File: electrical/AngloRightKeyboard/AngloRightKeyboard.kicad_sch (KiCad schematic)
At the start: 47 parts, among them J1 I2C, J2 TC2030-NL, U1 DRV5053VAQDBZR, U10 DRV5053VAQDBZR, U11 DRV5053VAQDBZR, U12 DRV5053VAQDBZR, U13 DRV5053VAQDBZR, U14 DRV5053VAQDBZR, U15 DRV5053VAQDBZR, U16 STM32L072CBTx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

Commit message: Update titles in kicad files
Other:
- title: MIDI Concertina Controller -> MIDI Anglo Right Keyboard
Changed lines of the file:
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@@
 	(paper "USLedger")
 	(title_block
-		(title "MIDI Concertina Controller")
+		(title "MIDI Anglo Right Keyboard")
 		(date "2025-10-01")
 		(rev "1")

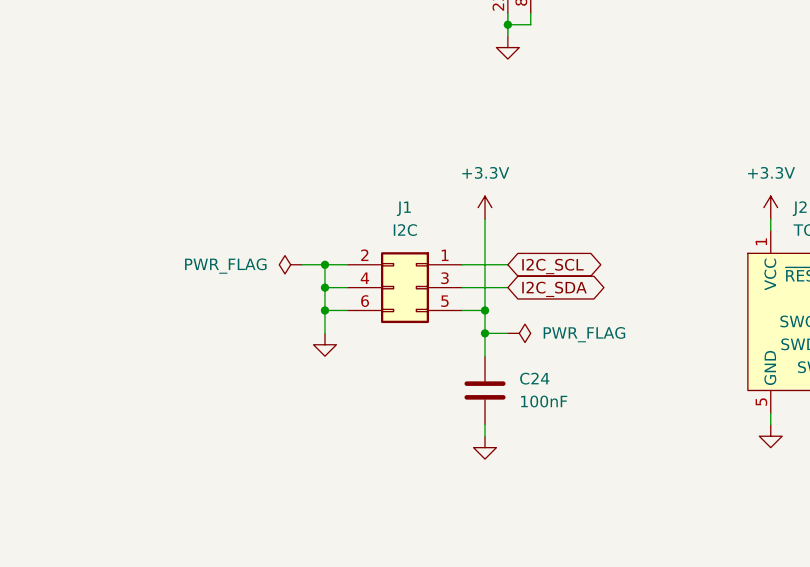
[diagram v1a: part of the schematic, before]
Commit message: Change i2c cable pinout to keep signals between grounds
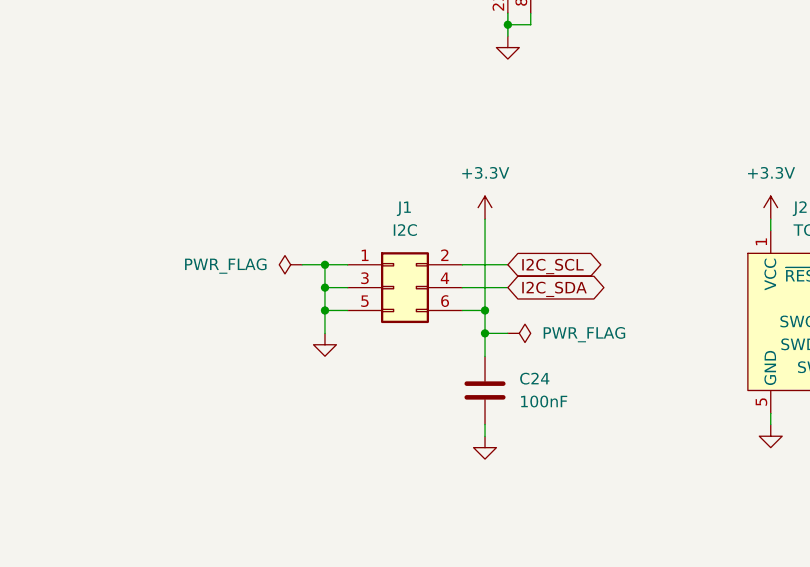
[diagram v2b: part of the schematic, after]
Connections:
- net +3.3V: now also J1.6 (Pin_6); no longer J1.5 (Pin_5)
- net GND: now also J1.1 (Pin_1), J1.3 (Pin_3), J1.5 (Pin_5); no longer J1.2 (Pin_2), J1.4 (Pin_4), J1.6 (Pin_6)
- net I2C_SCL: now also J1.2 (Pin_2); no longer J1.1 (Pin_1)
- net I2C_SDA: now also J1.4 (Pin_4); no longer J1.3 (Pin_3)
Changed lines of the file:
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@@
 	(symbol
 		(lib_id "Connector_Generic:Conn_02x03_Odd_Even")
-		(at 96.52 179.07 0)
-		(mirror y)
+		(at 93.98 179.07 0)
 		(unit 1)
 		(exclude_from_sim no)
@@
 		(on_board yes)
 		(dnp no)
-		(fields_autoplaced yes)
 		(property "Reference" "J1"
 			(at 95.25 170.18 0)
@@
 		)
 		(property "Footprint" "MidiConcertina:Wuerth_WR-WST_490107670612_2x03_P2.54mm_SKEDD"
-			(at 96.52 179.07 0)
+			(at 93.98 179.07 0)
 			(effects
 				(font
@@
 		)
 		(property "Datasheet" ""
-			(at 96.52 179.07 0)
+			(at 93.98 179.07 0)
 			(effects
 				(font
@@
 		)
 		(property "Description" ""
-			(at 96.52 179.07 0)
+			(at 93.98 179.07 0)
 			(effects
 				(font
